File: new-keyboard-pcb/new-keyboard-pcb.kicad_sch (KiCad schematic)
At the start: 0 parts

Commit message: schematic done
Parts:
- added C1, C2: 22pF, Capacitor_SMD:C_0805_2012Metric_Pad1.18x1.45mm_HandSolder, symbol Device:C_Small
- added C3: 1µF, Capacitor_SMD:C_0805_2012Metric_Pad1.18x1.45mm_HandSolder, symbol Device:C_Small
- added C4, C5, C6, C7: 0.1µF, Capacitor_SMD:C_0805_2012Metric_Pad1.18x1.45mm_HandSolder, symbol Device:C_Small
- added CH1, CH2, CH3, CH4: choc_v1_SW_HS, Kailh_PG1353_Hotswap:Kailh-PG1353-Hotswap-1U, symbol PCM_marbastlib-choc:choc_v1_SW_HS_CPG135001S30
- added D1, D2, D3, D4: D_Small, Diode_SMD:D_SOD-123, symbol Device:D_Small
- added F1: 500mA, Fuse:Fuse_1206_3216Metric_Pad1.42x1.75mm_HandSolder, symbol Device:Polyfuse_Small
- added R1, R4: 10k, Resistor_SMD:R_0805_2012Metric_Pad1.20x1.40mm_HandSolder, symbol Device:R_Small
- added R2, R3: 22, Resistor_SMD:R_0805_2012Metric_Pad1.20x1.40mm_HandSolder, symbol Device:R_Small
- added SW1: SW_Push, random-keyboard-parts.pretty-master:SKQG-1155865, symbol Switch:SW_Push
- added U1: ATmega32U4-A, Package_QFP:TQFP-44_10x10mm_P0.8mm, symbol MCU_Microchip_ATmega:ATmega32U4-A
- added USB1: Molex-0548190589, random-keyboard-parts.pretty-master:Molex-0548190589, symbol random-keyboard-parts:Molex-0548190589
- added Y1: 16MHz, Crystal:Crystal_SMD_3225-4Pin_3.2x2.5mm_HandSoldering, symbol Device:Crystal_GND24_Small
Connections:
- new net: R1.2, SW1.2, U1.13 (~{RESET})
- new net: C2.2, U1.16 (XTAL2), Y1.3
- new net: C1.2, U1.17 (XTAL1), Y1.1
- new net: R3.2, U1.3 (D-)
- new net: R4.1, U1.33 (~{HWB}/PE2)
- new net: R2.2, U1.4 (D+)
- new net: C3.2, U1.6 (UCAP)
- new net: CH1.2, D1.2 (A)
- new net: CH3.2, D3.2 (A)
- new net: CH2.2, D2.2 (A)
- new net: CH4.2, D4.2 (A)
- new net +5V: C4.1, C5.1, C6.1, C7.1, F1.2, R1.1, U1.14 (VCC), U1.2 (UVCC), U1.24 (AVCC), U1.34 (VCC), U1.44 (AVCC), U1.7 (VBUS)
- new net COL0: CH1.1, CH3.1, U1.28 (PB4)
- new net COL1: CH2.1, CH4.1, U1.29 (PB5)
- new net D+: R2.1, USB1.3 (D+)
- new net D-: R3.1, USB1.4 (D-)
- new net GND: C1.1, C2.1, C3.1, C4.2, C5.2, C6.2, C7.2, R4.2, SW1.1, U1.15 (GND), U1.23 (GND), U1.35 (GND), U1.43 (GND), U1.5 (UGND), USB1.1 (GND), Y1.2, Y1.4
- new net ROW0: D1.1 (K), D2.1 (K), U1.27 (PD7)
- new net ROW1: D3.1 (K), D4.1 (K), U1.30 (PB6)
- new net VCC: F1.1, USB1.6 (SHIELD)

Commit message: return to masterzen
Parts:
- removed CH1, CH2, CH3, CH4: choc_v1_SW_HS, Kailh_PG1353_Hotswap:Kailh-PG1353-Hotswap-1U, symbol PCM_marbastlib-choc:choc_v1_SW_HS_CPG135001S30
- removed D1, D2, D3, D4: D_Small, Diode_SMD:D_SOD-123, symbol Device:D_Small
- removed SW1: SW_Push, random-keyboard-parts.pretty-master:SKQG-1155865, symbol Switch:SW_Push
- removed USB1: Molex-0548190589, random-keyboard-parts.pretty-master:Molex-0548190589, symbol random-keyboard-parts:Molex-0548190589
- added C8: 10µF, Capacitor_SMD:C_0805_2012Metric_Pad1.18x1.45mm_HandSolder, symbol Device:C_Small
- added J1: AVR-ISP-6, symbol Connector:AVR-ISP-6
- added R5, R6: 5.1k, Resistor_SMD:R_0805_2012Metric_Pad1.20x1.40mm_HandSolder, symbol Device:R_Small
- added SW2: SW_Push_Dual, random-keyboard-parts.pretty-master:SKQG-1155865, symbol Switch:SW_Push_Dual
- added U2: PRTR5V0U2X, symbol random-keyboard-parts:PRTR5V0U2X
- added USB1: HRO-TYPE-C-31-M-12, symbol Type-C:HRO-TYPE-C-31-M-12
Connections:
- net +5V: now also C8.1, J1.2 (VCC)
- net D+: now also R2.2, U1.4 (D+); no longer R2.1
- net D-: now also R3.2, U1.3 (D-); no longer R3.1
- net GND: now also C8.2, J1.6 (GND), R5.2, R6.2, SW2.3, U2.1 (GND), USB1.1 (GND), USB1.12 (GND), USB1.13 (SHIELD)
- net VCC: now also U2.4 (VCC), USB1.11 (VBUS), USB1.2 (VBUS)
- net MOSI: now reaches U1.10 (PB2)
- net MOSI: now also J1.4 (MOSI)
- net MISO: now reaches U1.11 (PB3)
- net MISO: now also J1.1 (MISO)
- net RESET: now reaches R1.2, U1.13 (~{RESET})
- net RESET: now also J1.5 (~{RST}), SW2.2
- net XTAL2: now reaches C2.2, U1.16 (XTAL2), Y1.3
- net XTAL1: now reaches C1.2, U1.17 (XTAL1), Y1.1
- net SCK: now reaches U1.9 (PB1)
- net SCK: now also J1.3 (SCK)
- net COL0: no longer names the net of U1.28 (PB4)
- net COL1: no longer names the net of U1.29 (PB5)
- net ROW0: no longer names the net of U1.27 (PD7)
- net ROW1: no longer names the net of U1.30 (PB6)
- new net: R2.1, U2.2 (IO1), USB1.6 (DP1), USB1.8 (DP2)
- new net: R3.1, U2.3 (IO2), USB1.5 (DN2), USB1.7 (DN1)
- new net: R5.1, USB1.10 (CC2)
- new net: R6.1, USB1.4 (CC1)
- no-connect marks 0 -> 4
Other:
- moved on the sheet: C1, C2, C4, C5, C6, C7, F1, R1, Y1

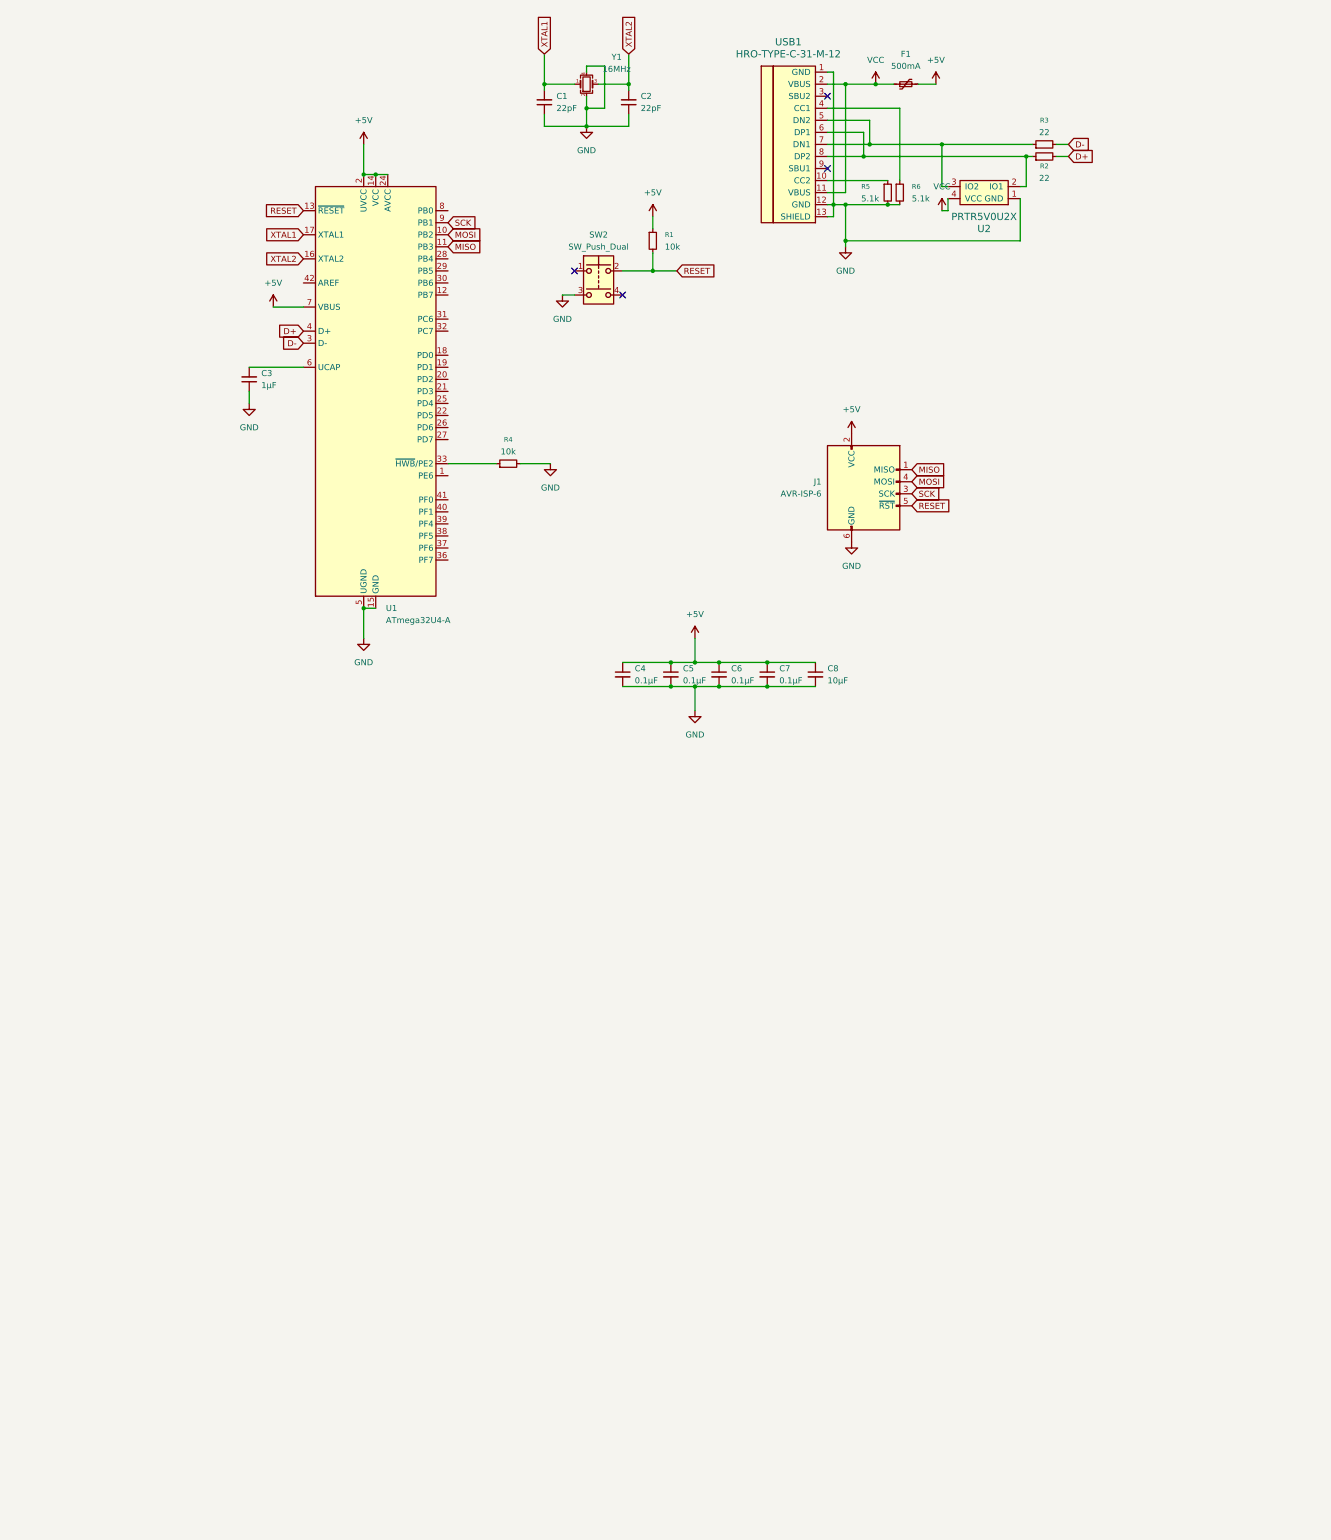
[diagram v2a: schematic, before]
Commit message: main keyboard switch placed
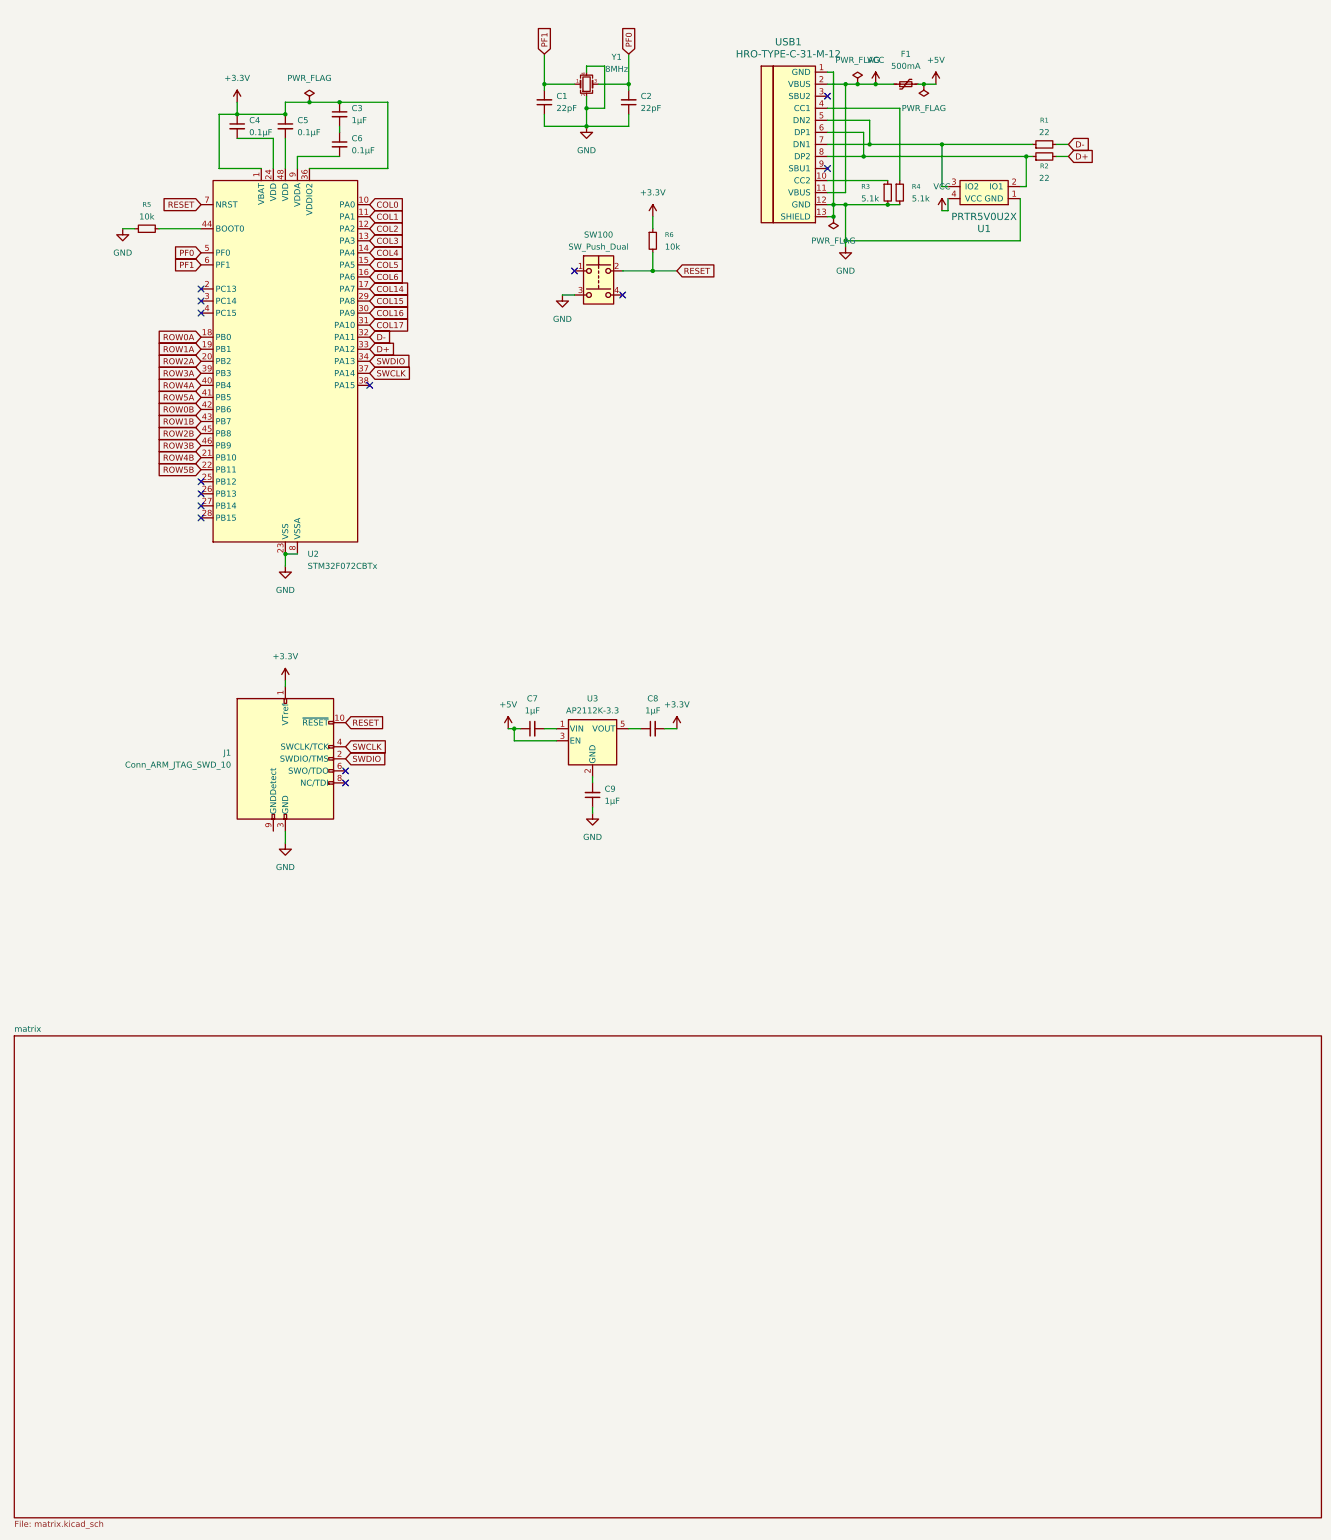
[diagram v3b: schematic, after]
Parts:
- removed J1: AVR-ISP-6, symbol Connector:AVR-ISP-6
- removed R4: 10k, Resistor_SMD:R_0805_2012Metric_Pad1.20x1.40mm_HandSolder, symbol Device:R_Small
- removed U1: ATmega32U4-A, Package_QFP:TQFP-44_10x10mm_P0.8mm, symbol MCU_Microchip_ATmega:ATmega32U4-A
- added C9: 1µF, Capacitor_SMD:C_0805_2012Metric_Pad1.18x1.45mm_HandSolder, symbol Device:C_Small
- added J1: Conn_ARM_JTAG_SWD_10, Connector_PinSocket_2.54mm:PinSocket_2x05_P2.54mm_Vertical, symbol Connector:Conn_ARM_JTAG_SWD_10
- added R5: 10k, Resistor_SMD:R_0805_2012Metric_Pad1.20x1.40mm_HandSolder, symbol Device:R_Small
- added U2: STM32F072CBTx, Package_QFP:LQFP-48_7x7mm_P0.5mm, symbol MCU_ST_STM32F0:STM32F072CBTx
- added U3: AP2112K-3.3, Package_TO_SOT_SMD:SOT-23-5, symbol Regulator_Linear:AP2112K-3.3
- C7: value 0.1µF -> 1µF
- C8: value 10µF -> 1µF
- U1: renamed from U2; footprint (none) -> random-keyboard-parts.pretty-master:SOT143B
- USB1: footprint (none) -> Type-C.pretty-master:HRO-TYPE-C-31-M-12-HandSoldering
- Y1: value 16MHz -> 8MHz
- renumbered R3 to R1, R5 to R3, R6 to R4, R1 to R6, SW2 to SW100
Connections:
- net +5V: now also U3.3 (EN); no longer C4.1, C5.1, C6.1, C8.1, R6.1
- net D+: now also U2.33 (PA12)
- net D-: now also U2.32 (PA11)
- net GND: now also C9.1, J1.3 (GND), J1.5 (GND), R5.1, U2.23 (VSS), U2.35 (VSS), U2.47 (VSS), U2.8 (VSSA); no longer C3.1, C4.2, C5.2, C6.2, C7.2, C8.2
- net RESET: now also J1.10 (~{RESET}), U2.7 (NRST)
- net at C3.2: now also C6.1
- net XTAL1 renamed PF1
- net PF1: now also U2.6 (PF1)
- net XTAL2 renamed PF0
- net PF0: now also U2.5 (PF0)
- new net: C4.2, U2.24 (VDD)
- new net: R5.2, U2.44 (BOOT0)
- new net: C5.2, U2.48 (VDD)
- new net: C6.2, U2.9 (VDDA)
- new net: C7.2, U3.1 (VIN)
- new net: C8.1, U3.5 (VOUT)
- new net: C9.2, U3.2 (GND)
- new net +3.3V: C3.1, C4.1, C5.1, C8.2, J1.1 (VTref), R6.1, U2.1 (VBAT), U2.36 (VDDIO2)
- new net COL0: U2.10 (PA0)
- new net COL1: U2.11 (PA1)
- new net COL14: U2.17 (PA7)
- new net COL15: U2.29 (PA8)
- new net COL16: U2.30 (PA9)
- new net COL17: U2.31 (PA10)
- new net COL2: U2.12 (PA2)
- new net COL3: U2.13 (PA3)
- new net COL4: U2.14 (PA4)
- new net COL5: U2.15 (PA5)
- new net COL6: U2.16 (PA6)
- new net ROW0A: U2.18 (PB0)
- new net ROW0B: U2.42 (PB6)
- new net ROW1A: U2.19 (PB1)
- new net ROW1B: U2.43 (PB7)
- new net ROW2A: U2.20 (PB2)
- new net ROW2B: U2.45 (PB8)
- new net ROW3A: U2.39 (PB3)
- new net ROW3B: U2.46 (PB9)
- new net ROW4A: U2.40 (PB4)
- new net ROW4B: U2.21 (PB10)
- new net ROW5A: U2.41 (PB5)
- new net ROW5B: U2.22 (PB11)
- new net SWCLK: J1.4 (SWCLK/TCK), U2.37 (PA14)
- new net SWDIO: J1.2 (SWDIO/TMS), U2.34 (PA13)
- no-connect marks 4 -> 14
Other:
- added sheet matrix (matrix.kicad_sch)

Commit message: midway correcting hotswap sockets
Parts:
- added J2: Conn_01x04_Socket, pogo_conn_4_pins:686L0421350120E, symbol Connector:Conn_01x04_Socket
- added J3: Conn_01x04_Pin, pogo_conn_4_pins:685L0421250110E, symbol Connector:Conn_01x04_Pin
- added J4, J6: Conn_01x03_Socket, pogo_conn_3_pins:685F0321351124E, symbol Connector:Conn_01x03_Socket
- added J5, J7: Conn_01x03_Pin, pogo_conn_3_pins:685F0321350124E, symbol Connector:Conn_01x03_Pin
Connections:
- net COL0: now also U2.12 (PA2); no longer U2.10 (PA0)
- net COL1: now also U2.13 (PA3); no longer U2.11 (PA1)
- net COL14: now also J3.4 (Pin_4); no longer U2.17 (PA7)
- net COL15: now also J3.3 (Pin_3); no longer U2.29 (PA8)
- net COL16: now also J3.2 (Pin_2); no longer U2.30 (PA9)
- net COL17: now also J3.1 (Pin_1); no longer U2.31 (PA10)
- net COL2: now also U2.14 (PA4); no longer U2.12 (PA2)
- net COL3: now also U2.15 (PA5); no longer U2.13 (PA3)
- net COL4: now also U2.16 (PA6); no longer U2.14 (PA4)
- net COL5: now also U2.17 (PA7); no longer U2.15 (PA5)
- net COL6: now also U2.18 (PB0); no longer U2.16 (PA6)
- net ROW0A: now also U2.19 (PB1); no longer U2.18 (PB0)
- net ROW0B: now also U2.20 (PB2), J4.3 (Pin_3); no longer U2.42 (PB6)
- net ROW1A: now also U2.46 (PB9); no longer U2.19 (PB1)
- net ROW1B: now also U2.21 (PB10), J4.2 (Pin_2); no longer U2.43 (PB7)
- net ROW2A: now also U2.45 (PB8); no longer U2.20 (PB2)
- net ROW2B: now also U2.28 (PB15), J4.1 (Pin_1); no longer U2.45 (PB8)
- net ROW3A: now also U2.43 (PB7); no longer U2.39 (PB3)
- net ROW3B: now also U2.29 (PA8), J6.3 (Pin_3); no longer U2.46 (PB9)
- net ROW4A: now also U2.42 (PB6); no longer U2.40 (PB4)
- net ROW4B: now also U2.30 (PA9), J6.2 (Pin_2); no longer U2.21 (PB10)
- net ROW5B: now also U2.31 (PA10), J6.1 (Pin_1); no longer U2.22 (PB11)
- net SWCLK: now also U2.25 (PB12); no longer U2.37 (PA14)
- net SWDIO: now also U2.26 (PB13); no longer U2.34 (PA13)
- net at U2.38 (PA15): now also J2.3 (Pin_3)
- new net: J2.4 (Pin_4), U2.37 (PA14)
- new net: J2.2 (Pin_2), U2.39 (PB3)
- new net: J2.1 (Pin_1), U2.40 (PB4)
- new net ROW0C: J5.3 (Pin_3)
- new net ROW1C: J5.2 (Pin_2)
- new net ROW2C: J5.1 (Pin_1)
- new net ROW3C: J7.3 (Pin_3)
- new net ROW4C: J7.2 (Pin_2)
- new net ROW5C: J7.1 (Pin_1)
